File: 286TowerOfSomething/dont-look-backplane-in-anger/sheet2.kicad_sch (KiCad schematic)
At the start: 4 parts, among them J1 Bus_ISA_16bit, J2 Bus_ISA_16bit, J3 Bus_ISA_16bit, J4 Bus_ISA_16bit

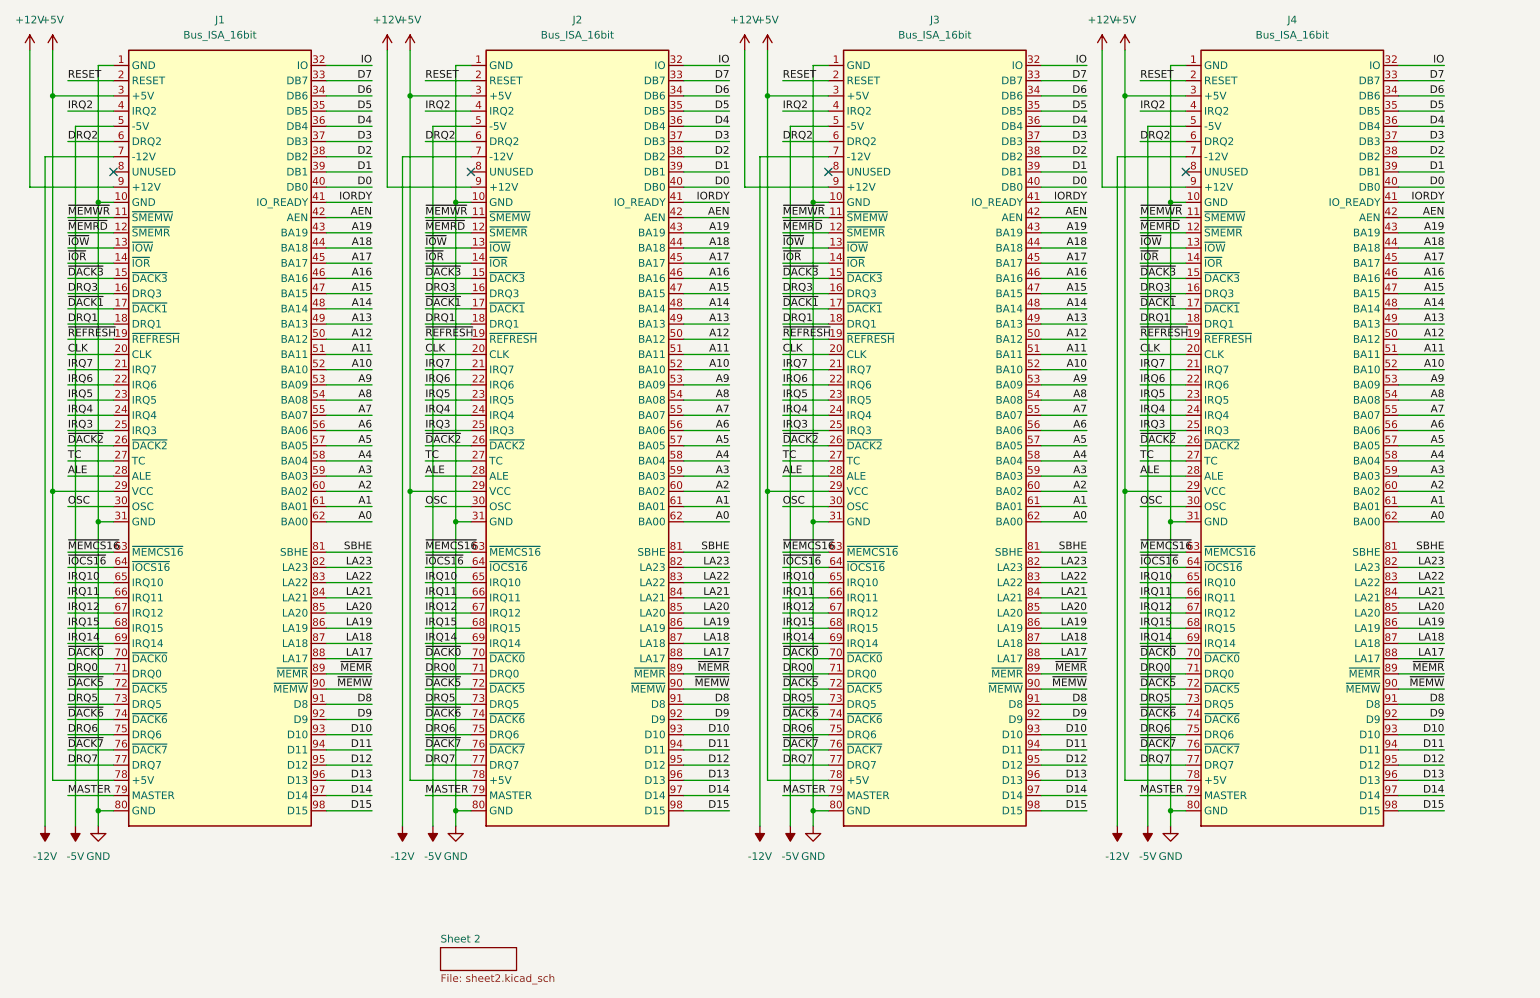
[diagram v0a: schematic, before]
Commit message: Cleaned up schematic, broke layout
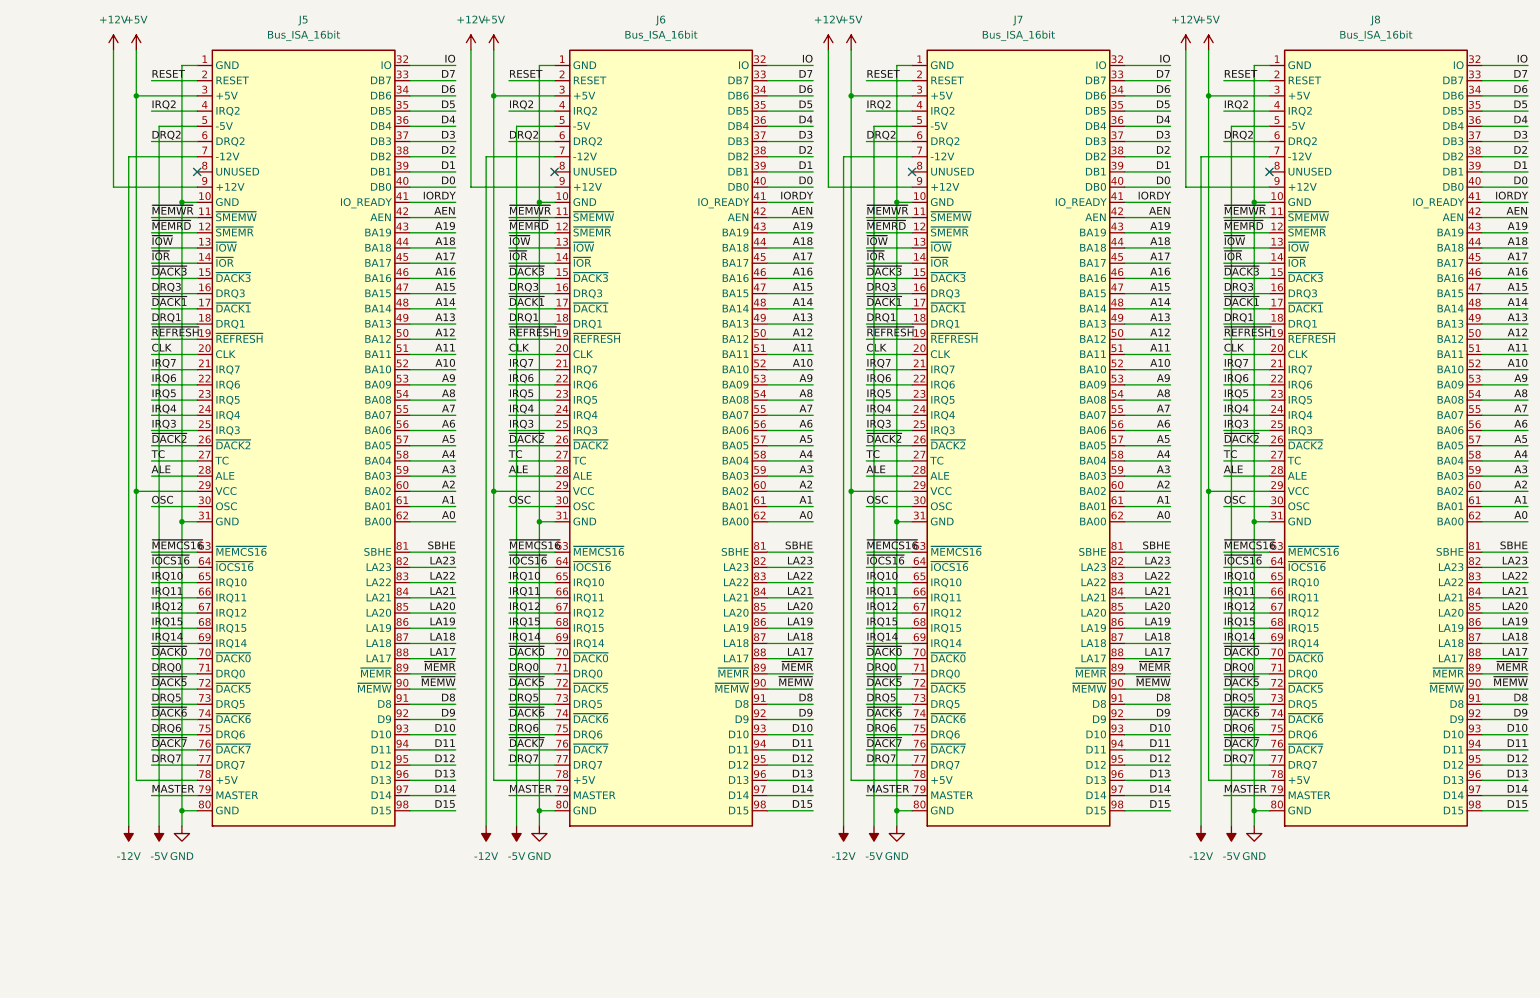
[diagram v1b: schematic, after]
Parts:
- removed J1, J2, J3, J4: Bus_ISA_16bit, pc-parts:645169-3, symbol Connector:Bus_ISA_16bit
- added J5, J6, J7, J8: Bus_ISA_16bit, pc-parts:645169-3, symbol Connector:Bus_ISA_16bit
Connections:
- net +12V: now also J5.9 (+12V), J6.9 (+12V), J7.9 (+12V), J8.9 (+12V)
- net +5V: now also J5.29 (VCC), J5.3 (+5V), J5.78 (+5V), J6.29 (VCC), J6.3 (+5V), J6.78 (+5V), J7.29 (VCC), J7.3 (+5V), J7.78 (+5V), J8.29 (VCC), J8.3 (+5V), J8.78 (+5V)
- net -12V: now also J5.7 (-12V), J6.7 (-12V), J7.7 (-12V), J8.7 (-12V)
- net -5V: now also J5.5 (-5V), J6.5 (-5V), J7.5 (-5V), J8.5 (-5V)
- net A0: now also J5.62 (BA00), J6.62 (BA00), J7.62 (BA00), J8.62 (BA00)
- net A1: now also J5.61 (BA01), J6.61 (BA01), J7.61 (BA01), J8.61 (BA01)
- net A10: now also J5.52 (BA10), J6.52 (BA10), J7.52 (BA10), J8.52 (BA10)
- net A11: now also J5.51 (BA11), J6.51 (BA11), J7.51 (BA11), J8.51 (BA11)
- net A12: now also J5.50 (BA12), J6.50 (BA12), J7.50 (BA12), J8.50 (BA12)
- net A13: now also J5.49 (BA13), J6.49 (BA13), J7.49 (BA13), J8.49 (BA13)
- net A14: now also J5.48 (BA14), J6.48 (BA14), J7.48 (BA14), J8.48 (BA14)
- net A15: now also J5.47 (BA15), J6.47 (BA15), J7.47 (BA15), J8.47 (BA15)
- net A16: now also J5.46 (BA16), J6.46 (BA16), J7.46 (BA16), J8.46 (BA16)
- net A17: now also J5.45 (BA17), J6.45 (BA17), J7.45 (BA17), J8.45 (BA17)
- net A18: now also J5.44 (BA18), J6.44 (BA18), J7.44 (BA18), J8.44 (BA18)
- net A19: now also J5.43 (BA19), J6.43 (BA19), J7.43 (BA19), J8.43 (BA19)
- net A2: now also J5.60 (BA02), J6.60 (BA02), J7.60 (BA02), J8.60 (BA02)
- net A3: now also J5.59 (BA03), J6.59 (BA03), J7.59 (BA03), J8.59 (BA03)
- net A4: now also J5.58 (BA04), J6.58 (BA04), J7.58 (BA04), J8.58 (BA04)
- net A5: now also J5.57 (BA05), J6.57 (BA05), J7.57 (BA05), J8.57 (BA05)
- net A6: now also J5.56 (BA06), J6.56 (BA06), J7.56 (BA06), J8.56 (BA06)
- net A7: now also J5.55 (BA07), J6.55 (BA07), J7.55 (BA07), J8.55 (BA07)
- net A8: now also J5.54 (BA08), J6.54 (BA08), J7.54 (BA08), J8.54 (BA08)
- net A9: now also J5.53 (BA09), J6.53 (BA09), J7.53 (BA09), J8.53 (BA09)
- net AEN: now also J5.42 (AEN), J6.42 (AEN), J7.42 (AEN), J8.42 (AEN)
- net ALE: now also J5.28 (ALE), J6.28 (ALE), J7.28 (ALE), J8.28 (ALE)
- net CLK: now also J5.20 (CLK), J6.20 (CLK), J7.20 (CLK), J8.20 (CLK)
- net D0: now also J5.40 (DB0), J6.40 (DB0), J7.40 (DB0), J8.40 (DB0)
- net D1: now also J5.39 (DB1), J6.39 (DB1), J7.39 (DB1), J8.39 (DB1)
- net D10: now also J5.93 (D10), J6.93 (D10), J7.93 (D10), J8.93 (D10)
- net D11: now also J5.94 (D11), J6.94 (D11), J7.94 (D11), J8.94 (D11)
- net D12: now also J5.95 (D12), J6.95 (D12), J7.95 (D12), J8.95 (D12)
- net D13: now also J5.96 (D13), J6.96 (D13), J7.96 (D13), J8.96 (D13)
- net D14: now also J5.97 (D14), J6.97 (D14), J7.97 (D14), J8.97 (D14)
- net D15: now also J5.98 (D15), J6.98 (D15), J7.98 (D15), J8.98 (D15)
- net D2: now also J5.38 (DB2), J6.38 (DB2), J7.38 (DB2), J8.38 (DB2)
- net D3: now also J5.37 (DB3), J6.37 (DB3), J7.37 (DB3), J8.37 (DB3)
- net D4: now also J5.36 (DB4), J6.36 (DB4), J7.36 (DB4), J8.36 (DB4)
- net D5: now also J5.35 (DB5), J6.35 (DB5), J7.35 (DB5), J8.35 (DB5)
- net D6: now also J5.34 (DB6), J6.34 (DB6), J7.34 (DB6), J8.34 (DB6)
- net D7: now also J5.33 (DB7), J6.33 (DB7), J7.33 (DB7), J8.33 (DB7)
- net D8: now also J5.91 (D8), J6.91 (D8), J7.91 (D8), J8.91 (D8)
- net D9: now also J5.92 (D9), J6.92 (D9), J7.92 (D9), J8.92 (D9)
- net DRQ0: now also J5.71 (DRQ0), J6.71 (DRQ0), J7.71 (DRQ0), J8.71 (DRQ0)
- net DRQ1: now also J5.18 (DRQ1), J6.18 (DRQ1), J7.18 (DRQ1), J8.18 (DRQ1)
- net DRQ2: now also J5.6 (DRQ2), J6.6 (DRQ2), J7.6 (DRQ2), J8.6 (DRQ2)
- net DRQ3: now also J5.16 (DRQ3), J6.16 (DRQ3), J7.16 (DRQ3), J8.16 (DRQ3)
- net DRQ5: now also J5.73 (DRQ5), J6.73 (DRQ5), J7.73 (DRQ5), J8.73 (DRQ5)
- net DRQ6: now also J5.75 (DRQ6), J6.75 (DRQ6), J7.75 (DRQ6), J8.75 (DRQ6)
- net DRQ7: now also J5.77 (DRQ7), J6.77 (DRQ7), J7.77 (DRQ7), J8.77 (DRQ7)
- net GND: now also J5.1 (GND), J5.10 (GND), J5.31 (GND), J5.80 (GND), J6.1 (GND), J6.10 (GND), J6.31 (GND), J6.80 (GND), J7.1 (GND), J7.10 (GND), J7.31 (GND), J7.80 (GND), J8.1 (GND), J8.10 (GND), J8.31 (GND), J8.80 (GND)
- net IO: now also J5.32 (IO), J6.32 (IO), J7.32 (IO), J8.32 (IO)
- net IORDY: now also J5.41 (IO_READY), J6.41 (IO_READY), J7.41 (IO_READY), J8.41 (IO_READY)
- net IRQ10: now also J5.65 (IRQ10), J6.65 (IRQ10), J7.65 (IRQ10), J8.65 (IRQ10)
- net IRQ11: now also J5.66 (IRQ11), J6.66 (IRQ11), J7.66 (IRQ11), J8.66 (IRQ11)
- net IRQ12: now also J5.67 (IRQ12), J6.67 (IRQ12), J7.67 (IRQ12), J8.67 (IRQ12)
- net IRQ14: now also J5.69 (IRQ14), J6.69 (IRQ14), J7.69 (IRQ14), J8.69 (IRQ14)
- net IRQ15: now also J5.68 (IRQ15), J6.68 (IRQ15), J7.68 (IRQ15), J8.68 (IRQ15)
- net IRQ2: now also J5.4 (IRQ2), J6.4 (IRQ2), J7.4 (IRQ2), J8.4 (IRQ2)
- net IRQ3: now also J5.25 (IRQ3), J6.25 (IRQ3), J7.25 (IRQ3), J8.25 (IRQ3)
- net IRQ4: now also J5.24 (IRQ4), J6.24 (IRQ4), J7.24 (IRQ4), J8.24 (IRQ4)
- net IRQ5: now also J5.23 (IRQ5), J6.23 (IRQ5), J7.23 (IRQ5), J8.23 (IRQ5)
- net IRQ6: now also J5.22 (IRQ6), J6.22 (IRQ6), J7.22 (IRQ6), J8.22 (IRQ6)
- net IRQ7: now also J5.21 (IRQ7), J6.21 (IRQ7), J7.21 (IRQ7), J8.21 (IRQ7)
- net LA17: now also J5.88 (LA17), J6.88 (LA17), J7.88 (LA17), J8.88 (LA17)
- net LA18: now also J5.87 (LA18), J6.87 (LA18), J7.87 (LA18), J8.87 (LA18)
- net LA19: now also J5.86 (LA19), J6.86 (LA19), J7.86 (LA19), J8.86 (LA19)
- net LA20: now also J5.85 (LA20), J6.85 (LA20), J7.85 (LA20), J8.85 (LA20)
- net LA21: now also J5.84 (LA21), J6.84 (LA21), J7.84 (LA21), J8.84 (LA21)
- net LA22: now also J5.83 (LA22), J6.83 (LA22), J7.83 (LA22), J8.83 (LA22)
- net LA23: now also J5.82 (LA23), J6.82 (LA23), J7.82 (LA23), J8.82 (LA23)
- net MASTER: now also J5.79 (MASTER), J6.79 (MASTER), J7.79 (MASTER), J8.79 (MASTER)
- net OSC: now also J5.30 (OSC), J6.30 (OSC), J7.30 (OSC), J8.30 (OSC)
- net RESET: now also J5.2 (RESET), J6.2 (RESET), J7.2 (RESET), J8.2 (RESET)
- net SBHE: now also J5.81 (SBHE), J6.81 (SBHE), J7.81 (SBHE), J8.81 (SBHE)
- net TC: now also J5.27 (TC), J6.27 (TC), J7.27 (TC), J8.27 (TC)
- net ~{DACK0}: now also J5.70 (~{DACK0}), J6.70 (~{DACK0}), J7.70 (~{DACK0}), J8.70 (~{DACK0})
- net ~{DACK1}: now also J5.17 (~{DACK1}), J6.17 (~{DACK1}), J7.17 (~{DACK1}), J8.17 (~{DACK1})
- net ~{DACK2}: now also J5.26 (~{DACK2}), J6.26 (~{DACK2}), J7.26 (~{DACK2}), J8.26 (~{DACK2})
- net ~{DACK3}: now also J5.15 (~{DACK3}), J6.15 (~{DACK3}), J7.15 (~{DACK3}), J8.15 (~{DACK3})
- net ~{DACK5}: now also J5.72 (~{DACK5}), J6.72 (~{DACK5}), J7.72 (~{DACK5}), J8.72 (~{DACK5})
- net ~{DACK6}: now also J5.74 (~{DACK6}), J6.74 (~{DACK6}), J7.74 (~{DACK6}), J8.74 (~{DACK6})
- net ~{DACK7}: now also J5.76 (~{DACK7}), J6.76 (~{DACK7}), J7.76 (~{DACK7}), J8.76 (~{DACK7})
- net ~{IOCS16}: now also J5.64 (~{IOCS16}), J6.64 (~{IOCS16}), J7.64 (~{IOCS16}), J8.64 (~{IOCS16})
- net ~{IOR}: now also J5.14 (~{IOR}), J6.14 (~{IOR}), J7.14 (~{IOR}), J8.14 (~{IOR})
- net ~{IOW}: now also J5.13 (~{IOW}), J6.13 (~{IOW}), J7.13 (~{IOW}), J8.13 (~{IOW})
- net ~{MEMCS16}: now also J5.63 (~{MEMCS16}), J6.63 (~{MEMCS16}), J7.63 (~{MEMCS16}), J8.63 (~{MEMCS16})
- net ~{MEMRD}: now also J5.12 (~{SMEMR}), J6.12 (~{SMEMR}), J7.12 (~{SMEMR}), J8.12 (~{SMEMR})
- net ~{MEMR}: now also J5.89 (~{MEMR}), J6.89 (~{MEMR}), J7.89 (~{MEMR}), J8.89 (~{MEMR})
- net ~{MEMWR}: now also J5.11 (~{SMEMW}), J6.11 (~{SMEMW}), J7.11 (~{SMEMW}), J8.11 (~{SMEMW})
- net ~{MEMW}: now also J5.90 (~{MEMW}), J6.90 (~{MEMW}), J7.90 (~{MEMW}), J8.90 (~{MEMW})
- net ~{REFRESH}: now also J5.19 (~{REFRESH}), J6.19 (~{REFRESH}), J7.19 (~{REFRESH}), J8.19 (~{REFRESH})
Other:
- removed sheet Sheet 2
